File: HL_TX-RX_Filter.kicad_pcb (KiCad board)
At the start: 2 copper layers, 100 x 100 mm, 201 parts, among them J1 CNR1, J10 To Rx in, J2 CNR3, J3 Antenna, J4 CNR2, J5 CNR4, J6 From Tx, J7 ICSP, J8 SCL SDA, J9 Input1, Q1 2N7002, Q2 2N7002, Q3 2N7002, Q4 2N7002, Q5 2N7002, Q6 2N7002, Q7 2N7002, Q8 2N7002, U1 ATMEGA328-AU, U10 PE4259, U11 PE4259, U12 PE4259, U2 PE4259, U3 PE4259, U4 PE4259, U5 PE4259, U6 PE4259, U7 PE4259, U8 PE4259, U9 PE4259

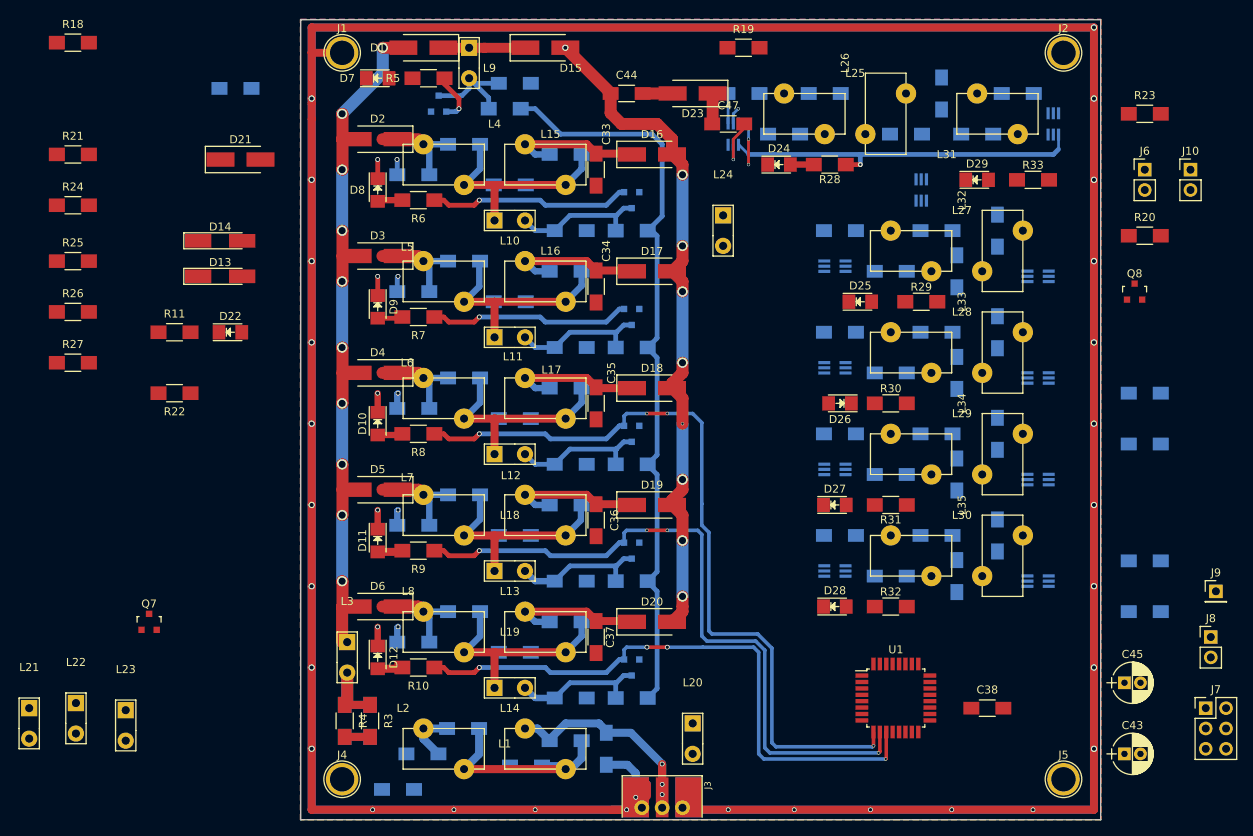
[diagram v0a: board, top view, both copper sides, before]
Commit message: Further progress on Filter switching lines
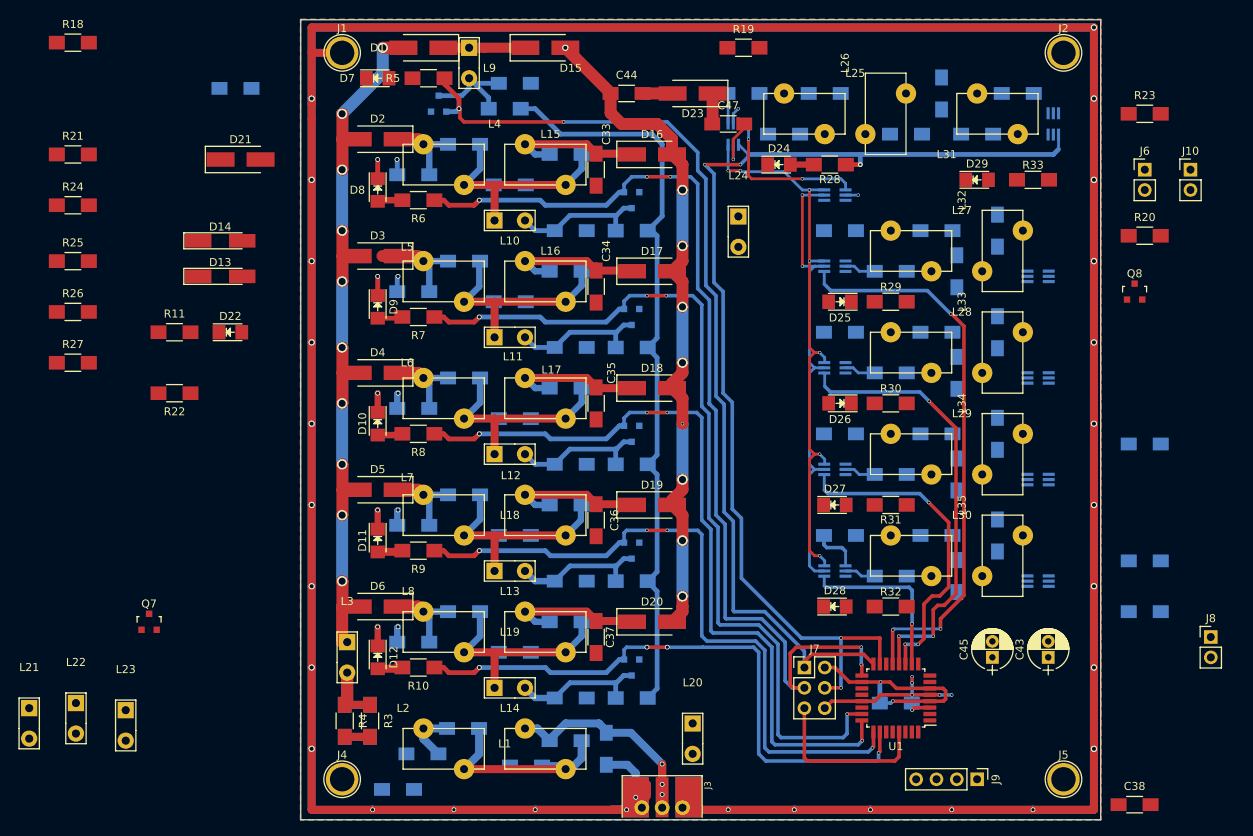
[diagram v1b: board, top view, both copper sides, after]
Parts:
- J9: value Input1 -> CONN_01X04; footprint Pin_Headers:Pin_Header_Straight_1x01_Pitch2.54mm -> Pin_Headers:Pin_Header_Straight_1x04_Pitch2.54mm
- moved J7 50.4 mm to (188.0, 141.0)
- moved C42 49.7 mm to (199.4, 145.4)
- moved J9 38.0 mm to (209.6, 154.9), turned to 270 degrees
- moved C38 22.0 mm to (229.2, 158.1)
- moved C45 16.8 mm to (211.5, 139.7), turned to 90 degrees
- moved C43 15.4 mm to (218.4, 139.7), turned to 90 degrees
- moved U3 10.8 mm to (191.8, 81.9), turned to 180 degrees
- moved R29 3.81 mm to (198.8, 95.2)
- moved D25 2.54 mm to (192.4, 95.2), turned to 180 degrees
- moved L24 1.91 mm to (179.7, 84.6)
- turned U1 to 180 degrees
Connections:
- net Net-(J8-Pad1) renamed /SDA
- net Net-(J8-Pad2) renamed /SCL
- net Net-(U1-Pad30) renamed /IO_1
- net Net-(U1-Pad31) renamed /IO_2
- J7 pad 1: /I3 -> /T0
- J7 pad 3: /I4 -> /T17
- J7 pad 4: /I2 -> /R1
- U1 pad 1: /T17 -> /I3
- U1 pad 10: /T80 -> /R5
- U1 pad 11: /T160 -> /R4
- U1 pad 12: /R0 -> /R3
- U1 pad 13: /R1 -> /R2
- U1 pad 14: /I1 -> /R0
- U1 pad 15: /I2 -> /R1
- U1 pad 16: /I3 -> /T0
- U1 pad 17: /I4 -> /T17
- U1 pad 2: /T30 -> /I2
- U1 pad 23: /R5 -> /T30
- U1 pad 24: /R4 -> /T40
- U1 pad 25: /R3 -> /T80
- U1 pad 26: /R2 -> /T160
- U1 pad 32: /T0 -> /I4
- U1 pad 7: /Tptt -> /I1
- U1 pad 9: /T40 -> /Tptt
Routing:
- net /T0: track 6.30 -> 121.4 mm, vias 1 -> 2
- net /T17: track 25.8 -> 127.5 mm, vias 1 -> 5
- net 3V3: track 0.00 -> 100.1 mm, vias 0 -> 9
- net /R1: track 45.7 -> 137.3 mm, vias 1 -> 5
- net /T30: track 25.2 -> 110.4 mm, vias 1 -> 4
- net /R2: track 0.00 -> 70.6 mm, vias 0 -> 3
- net Net-(J10-Pad1): track 0.00 -> 57.8 mm, vias 0 -> 2
- net /R3: track 0.00 -> 55.7 mm, vias 0 -> 3
- net GND: track 809.6 -> 853.6 mm, vias 40 -> 47
- net /R4: track 0.00 -> 40.6 mm, vias 0 -> 3
- net /R5: track 0.00 -> 21.6 mm, vias 0 -> 1
- net /RESET: track 0.00 -> 21.5 mm
- net Net-(U2-Pad3): track 5.99 -> 20.7 mm
- net Net-(C54-Pad1): track 0.00 -> 6.03 mm
- net Net-(C14-Pad1): track 12.6 -> 10.7 mm
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
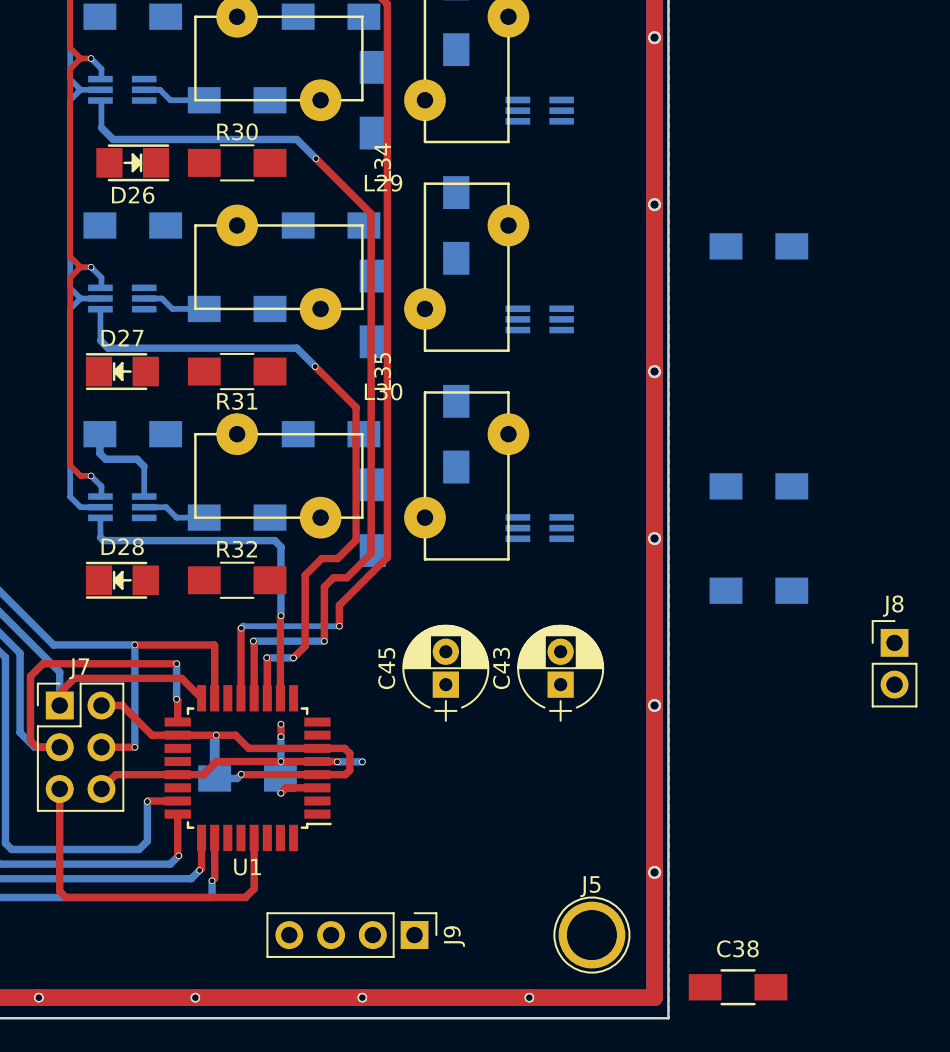
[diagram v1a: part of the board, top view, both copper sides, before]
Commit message: Placing inputs to microprocessor
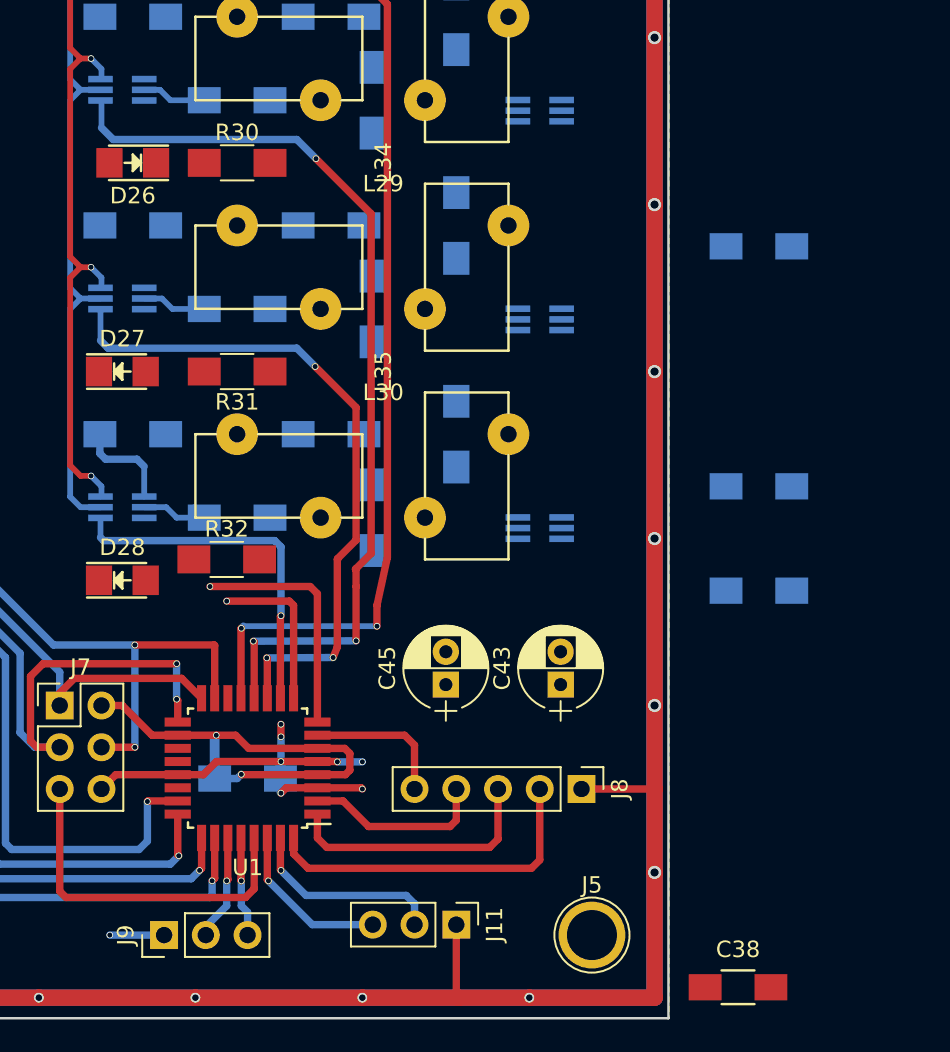
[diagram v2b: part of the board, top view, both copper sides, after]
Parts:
- added J11: CONN_01X03, Pin_Headers:Pin_Header_Straight_1x03_Pitch2.54mm, F.Cu at (212.1, 154.3)
- J8: value SCL SDA -> CONN_01X05; footprint Pin_Headers:Pin_Header_Straight_1x02_Pitch2.54mm -> Pin_Headers:Pin_Header_Straight_1x05_Pitch2.54mm
- J9: value CONN_01X04 -> SCL SDA; footprint Pin_Headers:Pin_Header_Straight_1x04_Pitch2.54mm -> Pin_Headers:Pin_Header_Straight_1x03_Pitch2.54mm
- moved J8 21.0 mm to (219.7, 146.1), turned to 270 degrees
- moved J9 15.2 mm to (194.3, 154.9), turned to 90 degrees
- moved R32 1.42 mm to (198.1, 132.1)
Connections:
- J8 pad 1: /SDA -> GND
- J8 pad 2: /SCL -> /I1
- J9 pad 1: /I1 -> GND
- J9 pad 2: /I2 -> /SDA
- J9 pad 3: /I3 -> /SCL
- U1 pad 1: /I3 -> /I2
- U1 pad 2: /I2 -> /I3
- U1 pad 30: /IO_1 -> /S1
- U1 pad 31: /IO_2 -> /S2
- U1 pad 32: /I4 -> /I1
- U1 pad 7: /I1 -> /I4
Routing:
- net /I1: track 0.00 -> 20.8 mm
- net /I2: track 0.00 -> 15.9 mm
- net GND: track 853.6 -> 868.9 mm, vias 47 -> 49
- net /Rptt: track 0.00 -> 14.5 mm, vias 0 -> 1
- net /S2: track 0.00 -> 12.2 mm, vias 0 -> 1
- net /I3: track 0.00 -> 11.2 mm
- net /S1: track 0.00 -> 10.1 mm, vias 0 -> 1
- net /Tptt: track 0.00 -> 9.83 mm, vias 0 -> 1
- net /I4: track 0.00 -> 8.83 mm
- net /SDA: track 0.00 -> 6.47 mm, vias 0 -> 1
- net /SCL: track 0.00 -> 6.08 mm, vias 0 -> 1
- net /R2: track 70.6 -> 71.7 mm
- net /R4: track 40.6 -> 41.4 mm
- net /R3: track 55.7 -> 56.5 mm

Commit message: Adjusted toroid sizes
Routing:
- net 3V3: track 100.1 -> 115.0 mm, vias 9 -> 10
- net GND: track 868.9 -> 881.8 mm

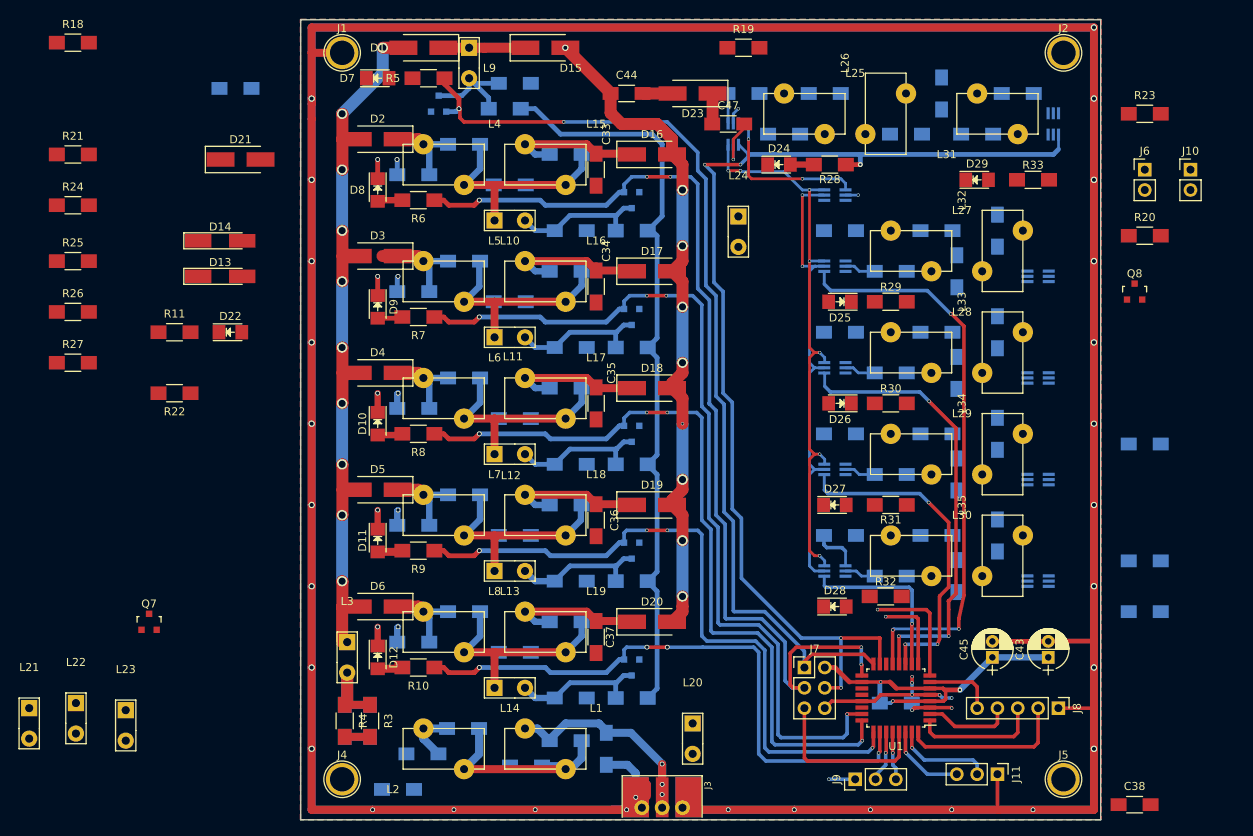
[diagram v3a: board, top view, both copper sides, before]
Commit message: Removed surplus choke etc from TX, RX switch
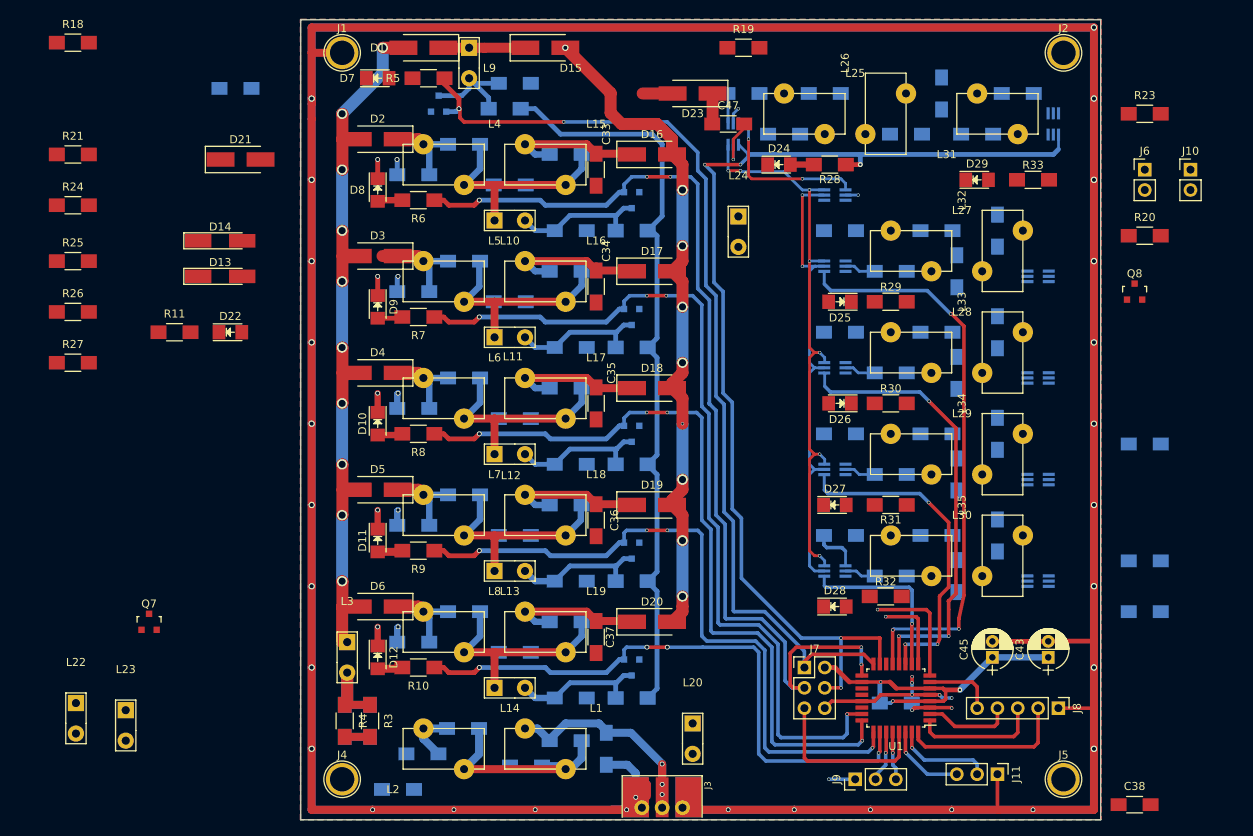
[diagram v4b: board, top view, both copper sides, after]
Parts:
- removed C44: C, Capacitors_SMD:C_1206_HandSoldering
- removed L21: Choke, Inductors_G:BalunCoreChoke
- removed R22: R, Resistors_SMD:R_1206_HandSoldering
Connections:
- D23 pad 2: Net-(C44-Pad2) -> Net-(C40-Pad2)
- L23 pad 1: Net-(L23-Pad1) -> 3V3
- L23 pad 2: 3V3 -> Net-(L23-Pad2)
- R25 pad 1: Net-(L23-Pad1) -> Net-(L23-Pad2)
- R25 pad 2: Net-(C44-Pad2) -> Net-(C40-Pad2)
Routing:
- net Net-(C44-Pad2): track 3.75 -> 0.00 mm
- net Net-(C40-Pad2): track 0.00 -> 3.75 mm

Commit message: Changed to Bourns chokes and progressed layout
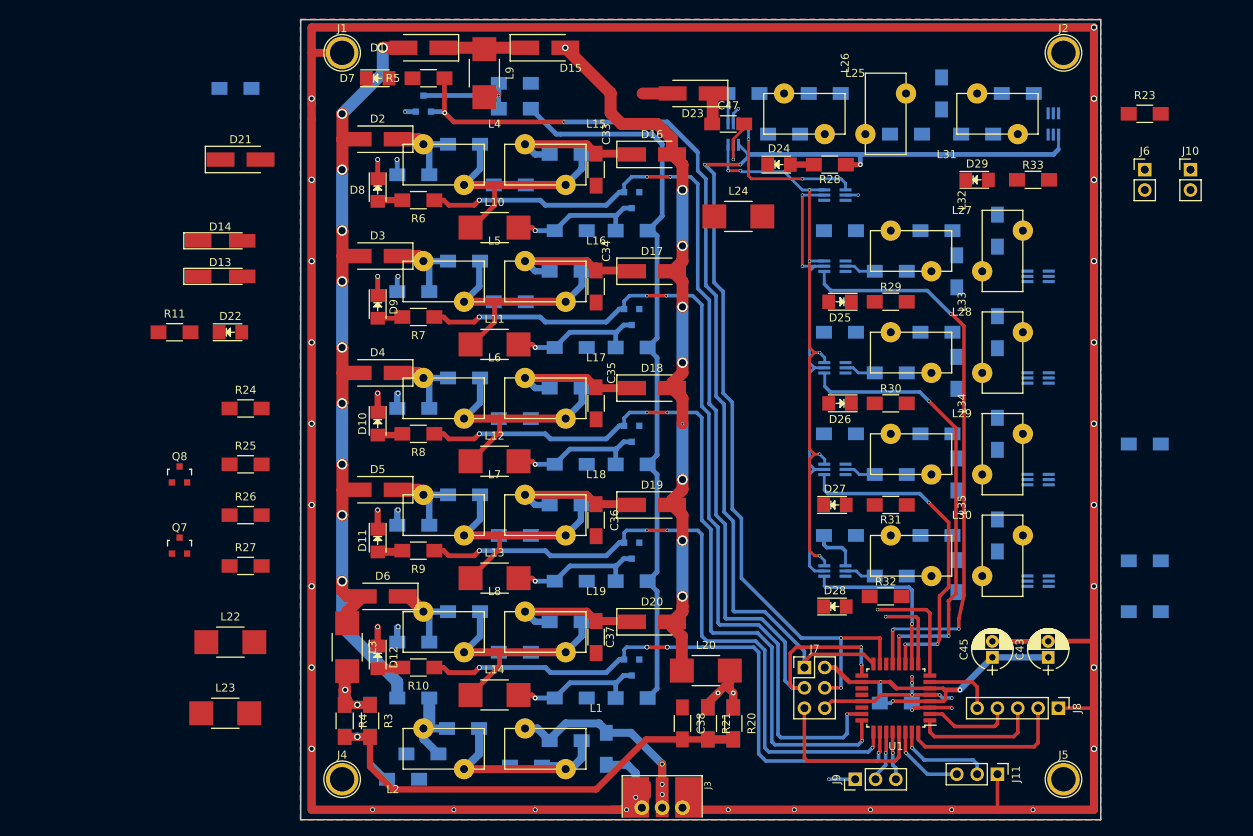
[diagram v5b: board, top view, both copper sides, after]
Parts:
- added C44: 0.1u, Capacitors_SMD:C_1206_HandSoldering, B.Cu at (139.1, 144.8)
- L10, L22, L23, L24: value Choke -> L; footprint Inductors_G:BalunCoreChoke -> Inductors_G:L_1812_HandSoldering
- L11, L12, L13, L14, L20, L3, L9: footprint Inductors_G:BalunCoreChoke -> Inductors_G:L_1812_HandSoldering
- R18, R19: moved to B.Cu
- moved Q8 121.5 mm to (109.9, 116.8)
- moved R18 116.4 mm to (175.9, 148.0), turned to 270 degrees
- moved R21 106.6 mm to (175.9, 148.0), turned to 270 degrees
- moved R19 84.5 mm to (179.1, 148.0), turned to 270 degrees
- moved R20 79.8 mm to (179.1, 148.0), turned to 270 degrees
- moved C38 57.4 mm to (172.7, 148.0), turned to 270 degrees
- moved R26 33.3 mm to (118.1, 121.9)
- moved R27 33.3 mm to (118.1, 128.3)
- moved R24 33.3 mm to (118.1, 108.6)
- moved R25 33.3 mm to (118.1, 115.6)
- moved L22 20.8 mm to (116.2, 137.8)
- moved L23 12.5 mm to (115.6, 146.7)
- moved Q7 10.3 mm to (109.9, 125.7)
- moved L20 6.81 mm to (175.6, 141.4)
- moved L9 3.70 mm to (148.0, 66.7), turned to 270 degrees
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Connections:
- D1 pad 2: Net-(C2-Pad1) -> Net-(C44-Pad2)
- D2 pad 2: Net-(C2-Pad1) -> Net-(C44-Pad2)
- D3 pad 2: Net-(C2-Pad1) -> Net-(C44-Pad2)
- D4 pad 2: Net-(C2-Pad1) -> Net-(C44-Pad2)
- D5 pad 2: Net-(C2-Pad1) -> Net-(C44-Pad2)
- D6 pad 2: Net-(C2-Pad1) -> Net-(C44-Pad2)
- L3 pad 1: Net-(C2-Pad1) -> Net-(C44-Pad2)
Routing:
- net Net-(C44-Pad2): track 0.00 -> 97.3 mm, vias 0 -> 10
- net Net-(C2-Pad1): track 86.3 -> 11.2 mm, vias 10 -> 0
- net Net-(C38-Pad2): track 6.35 -> 68.7 mm, vias 0 -> 1
- net Net-(L20-Pad2): track 0.00 -> 14.7 mm, vias 0 -> 2
- net Net-(C40-Pad1): track 84.5 -> 91.1 mm
- net Net-(C16-Pad2): track 32.0 -> 34.4 mm
- net Net-(C15-Pad2): track 32.0 -> 34.4 mm
- net Net-(C14-Pad2): track 32.0 -> 34.4 mm
- net Net-(C13-Pad2): track 31.4 -> 33.7 mm
- net Net-(C12-Pad2): track 31.4 -> 33.7 mm
- net Net-(C13-Pad1): track 12.6 -> 10.7 mm
- net GND: track 881.8 -> 883.1 mm, vias 49 -> 50
- net Net-(C46-Pad1): track 93.7 -> 92.4 mm
- net Net-(C17-Pad1): track 14.3 -> 15.2 mm, vias 0 -> 1
- net Net-(L3-Pad2): track 14.7 -> 13.7 mm, vias 0 -> 2
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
